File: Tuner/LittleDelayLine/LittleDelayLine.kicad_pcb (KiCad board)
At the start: 2 copper layers, 100 x 100 mm, 115 parts, among them J1 Conn_Coaxial, J10 Conn_Coaxial, J11 Conn_02x05_Odd_Even, J12 Conn_01x01, J13 Conn_01x01, J14 Conn_01x01, J15 Conn_01x01, J16 Conn_01x01, J17 Conn_Coaxial, J18 Conn_01x01, J19 Conn_01x01, J2 Conn_Coaxial, J20 Conn_01x01, J21 Conn_01x01, J22 Conn_Coaxial, J23 Conn_Coaxial, J24 Conn_Coaxial, J25 Conn_01x01, J26 Conn_01x01, J27 Conn_01x01, J28 Conn_01x01, J3 Conn_Coaxial, J4 Conn_Coaxial, J5 Conn_Coaxial, J6 Conn_Coaxial, J7 Conn_Coaxial, J8 Conn_Coaxial, J9 Conn_Coaxial, P10 Conn_01x01, P11 Conn_01x01, P12 Conn_01x01, P2 Conn_01x01, P3 Conn_01x01, P4 Conn_01x01, P5 Conn_01x01, P6 Conn_01x01, P7 Conn_01x01, P8 Conn_01x01, P9 Conn_01x01, U1 MCP23008, U2 ULN2803A

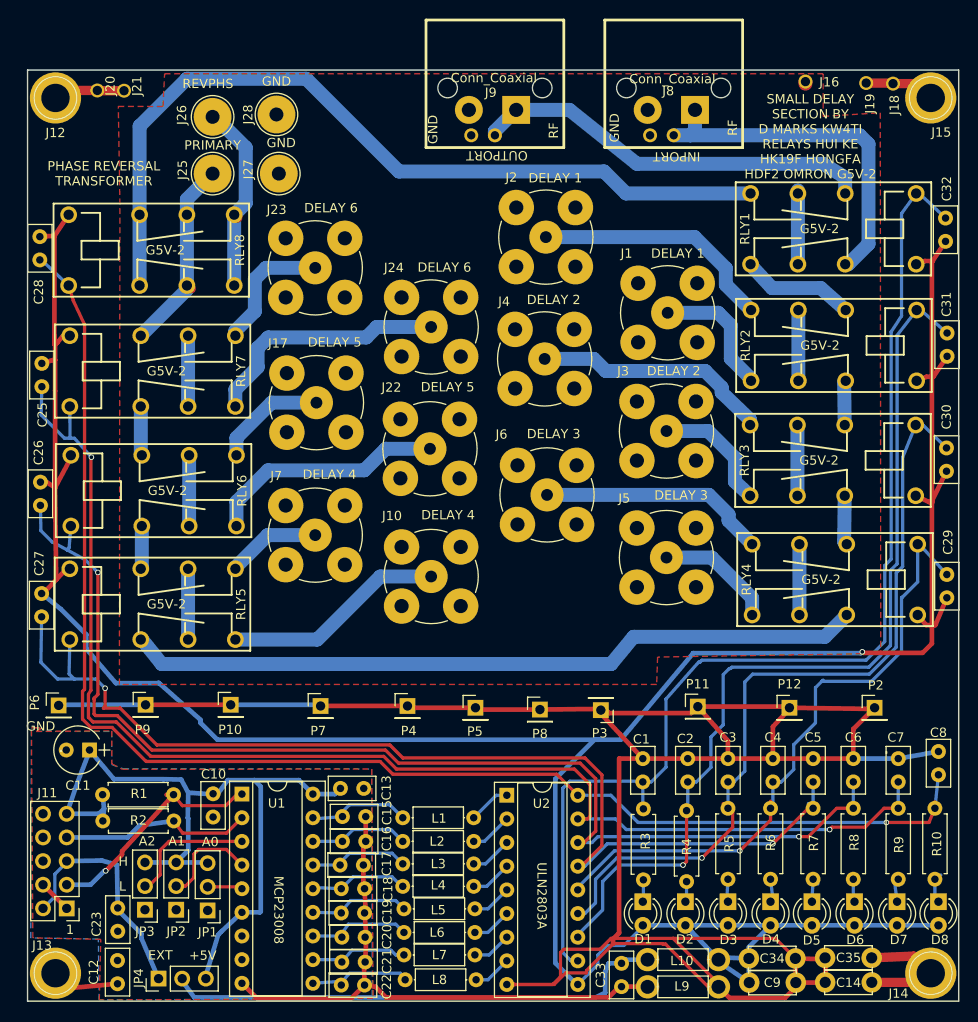
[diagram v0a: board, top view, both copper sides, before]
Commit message: Fixed spacing between BNC connectors in Delay Lines
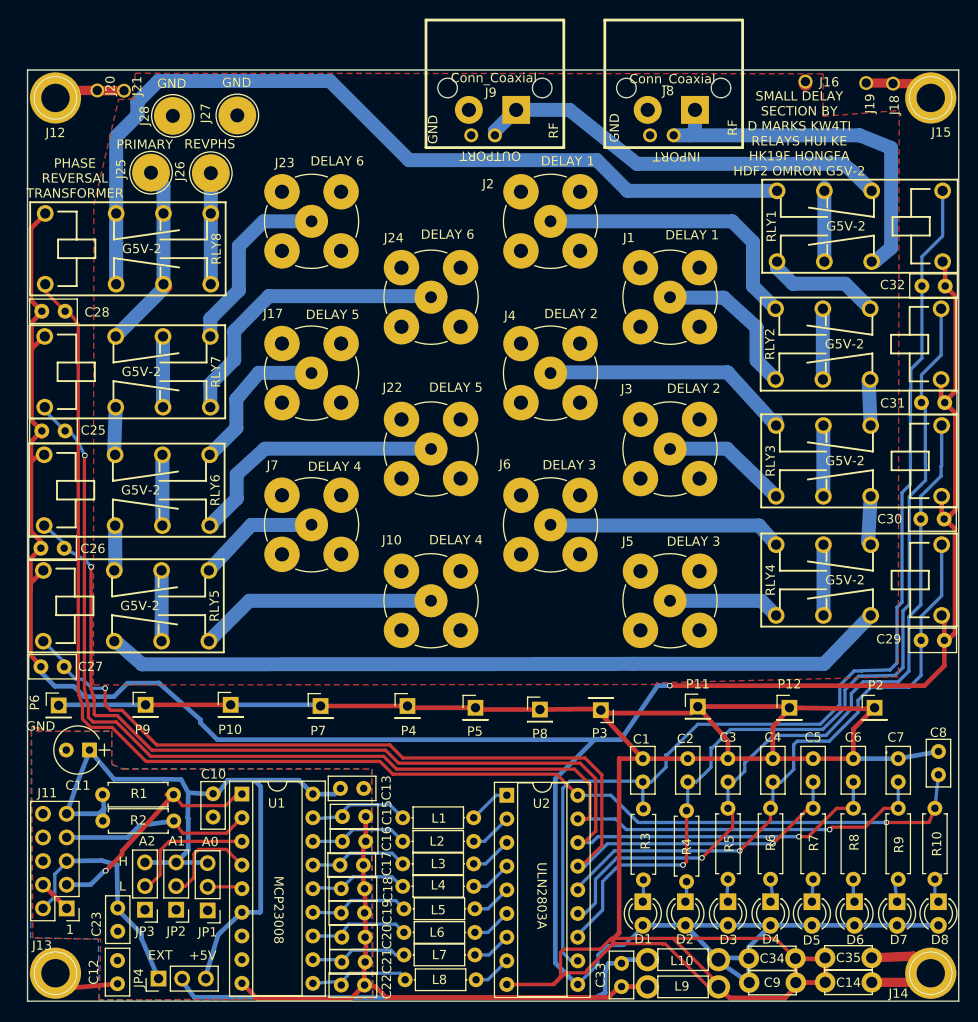
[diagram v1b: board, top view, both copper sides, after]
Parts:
- moved J28 11.1 mm to (65.6, 54.9)
- moved C28 8.02 mm to (51.5, 75.9), turned to 0 degrees
- moved C27 7.86 mm to (51.4, 114.1), turned to 0 degrees
- moved J27 7.68 mm to (72.5, 54.9)
- moved C25 7.25 mm to (51.5, 88.8), turned to 0 degrees
- moved C26 7.10 mm to (51.4, 101.4), turned to 0 degrees
- moved J25 6.62 mm to (63.3, 61.0)
- moved J26 6.05 mm to (69.7, 61.1)
- moved C30 5.14 mm to (148.4, 98.2), turned to 180 degrees
- moved J23 5.01 mm to (80.5, 66.2)
- moved C31 4.98 mm to (148.5, 85.7), turned to 180 degrees
- moved C32 4.80 mm to (148.6, 73.2), turned to 180 degrees
- moved J5 4.65 mm to (119.0, 107.0)
- moved C29 4.58 mm to (148.5, 111.3), turned to 180 degrees
- moved J6 3.24 mm to (106.2, 98.8)
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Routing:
- net RLY5: track 118.7 -> 109.8 mm
- net Net-(J26-Pad1): track 20.4 -> 12.1 mm
- net RLY7: track 143.3 -> 136.6 mm
- net Net-(J23-Pad1): track 13.9 -> 20.6 mm
- net RLY6: track 127.2 -> 121.7 mm
- net RFTHRU: track 89.9 -> 95.0 mm
- net Net-(J24-Pad1): track 26.8 -> 31.8 mm
- net Net-(RLY4-Pad2): track 79.4 -> 84.4 mm
- net RLYPWR: track 320.3 -> 315.7 mm
- net Net-(J2-Pad1): track 26.3 -> 30.8 mm
- net Net-(J17-Pad1): track 12.0 -> 16.4 mm
- net RLY3: track 86.7 -> 82.7 mm
- net Net-(J22-Pad1): track 25.7 -> 29.0 mm
- net Net-(J7-Pad1): track 10.2 -> 13.4 mm
- net Net-(J1-Pad1): track 14.2 -> 17.1 mm
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
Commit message: JLCPCB order 2019-03-25
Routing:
- net GND: track 68.2 -> 233.2 mm, vias 0 -> 24

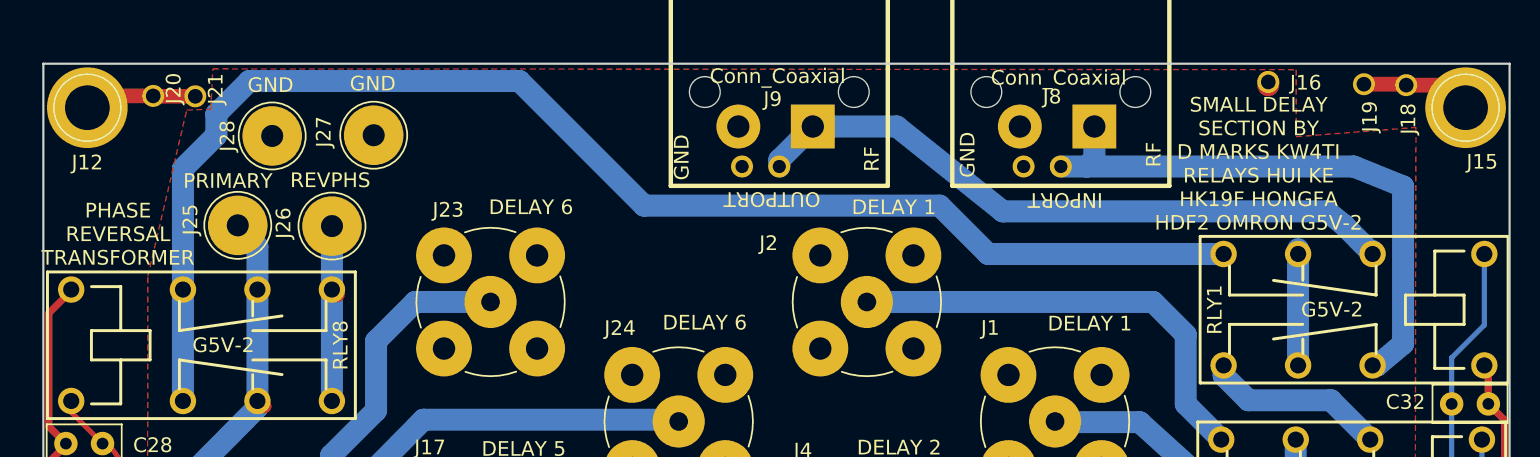
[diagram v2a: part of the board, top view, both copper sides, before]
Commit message: Added extra capacitors between relay power and ground posts
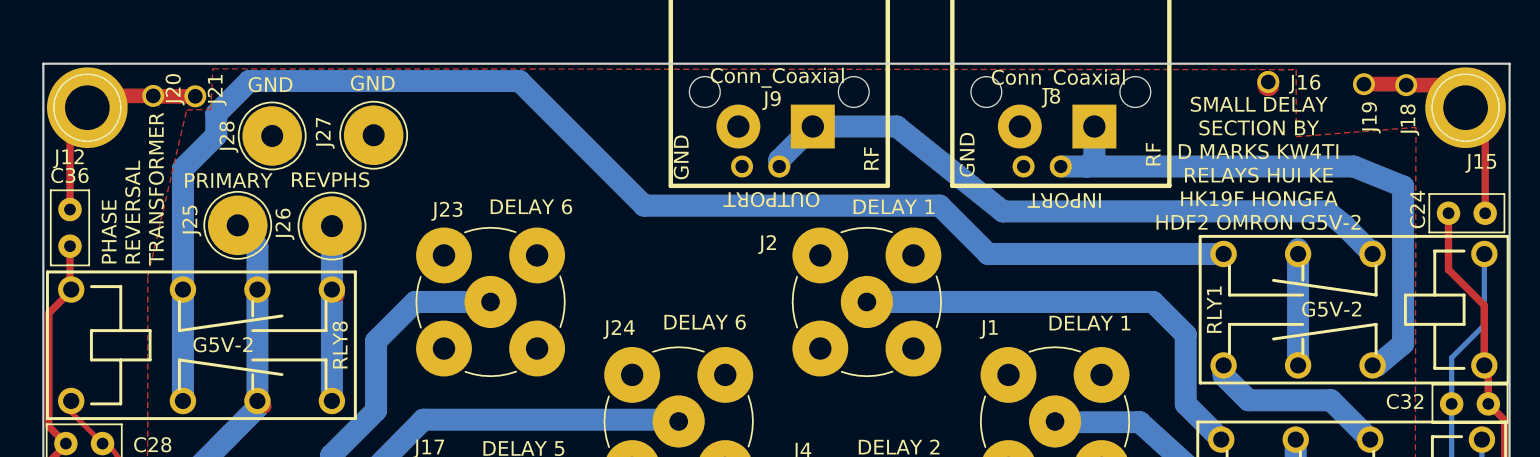
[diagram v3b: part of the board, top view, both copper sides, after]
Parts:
- added C24: 10 nF, Capacitors_THT:C_Disc_D5.0mm_W2.5mm_P2.50mm, F.Cu at (148.3, 60.2)
- added C36: 10 nF, Capacitors_THT:C_Disc_D5.0mm_W2.5mm_P2.50mm, F.Cu at (51.8, 59.9)
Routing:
- net RLYPWR: track 315.7 -> 330.1 mm
- net Net-(C24-Pad1): track 8.59 -> 16.3 mm
- net Net-(C36-Pad1): track 9.29 -> 16.7 mm

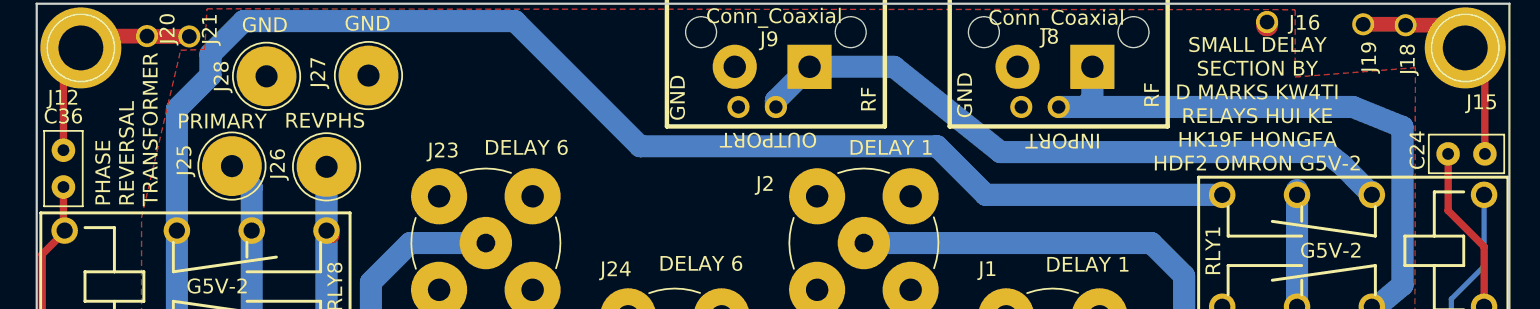
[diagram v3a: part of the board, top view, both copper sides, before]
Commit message: Added extra mounting holes to ground ReversibleLittleSection
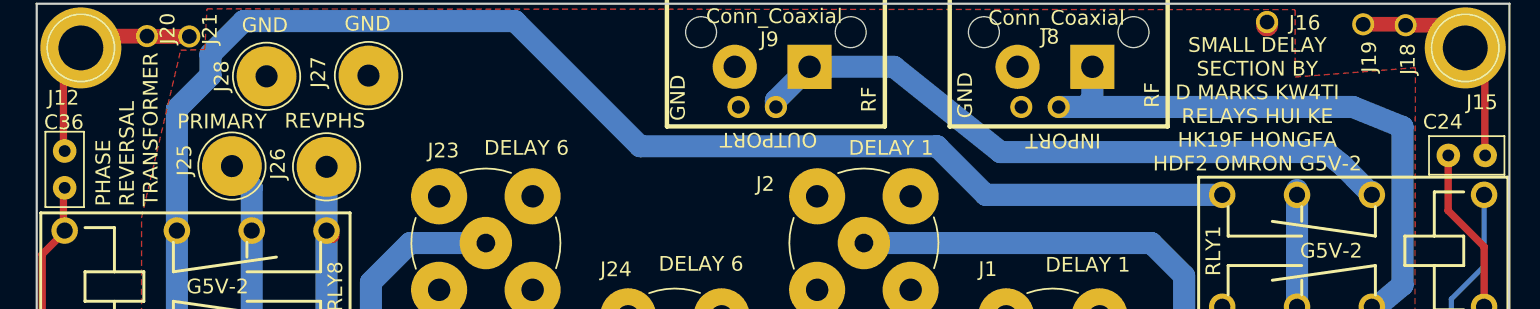
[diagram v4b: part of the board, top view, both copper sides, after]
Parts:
- C24, C36: value 10 nF -> NC
- moved C24 0.10 mm to (148.3, 60.3)
- moved C36 0.10 mm to (51.9, 60.0)
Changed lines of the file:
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@@
   )
   (setup
-    (last_trace_width 0.5)
+    (last_trace_width 0.25)
     (user_trace_width 0.35)
     (user_trace_width 0.5)
@@
   )
   (module Capacitors_THT:C_Disc_D5.0mm_W2.5mm_P2.50mm (layer F.Cu)
-    (at 148.336 60.198 180)
+    (at 148.35 60.3 180)
     (descr "C, Disc series, Radial, pin pitch=2.50mm, , diameter*width=5*2.5mm^2, Capacitor, http://cdn-reichelt.de/documents/datenblatt/B300/DS_KERKO_TC.pdf")
     (tags "C Disc series Radial pin pitch 2.50mm  diameter 5mm width 2.5mm Capacitor")
-    (fp_text reference C24 (at 4.572 0.254 270) (layer F.SilkS)
+    (fp_text reference C24 (at 2.875 2.275 180) (layer F.SilkS)
       (effects (font (size 1 1) (thickness 0.15)))
     )
-    (fp_text value "10 nF" (at 1.25 2.56 180) (layer F.Fab)
+    (fp_text value NC (at 1.25 2.56 180) (layer F.Fab)
       (effects (font (size 1 1) (thickness 0.15)))
     )
@@
   )
   (module Capacitors_THT:C_Disc_D5.0mm_W2.5mm_P2.50mm (layer F.Cu)
-    (at 51.816 59.944 270)
+    (at 51.9 60 270)
     (descr "C, Disc series, Radial, pin pitch=2.50mm, , diameter*width=5*2.5mm^2, Capacitor, http://cdn-reichelt.de/documents/datenblatt/B300/DS_KERKO_TC.pdf")
     (tags "C Disc series Radial pin pitch 2.50mm  diameter 5mm width 2.5mm Capacitor")
-    (fp_text reference C36 (at -2.286 0 360) (layer F.SilkS)
+    (fp_text reference C36 (at -1.95 0.05 360) (layer F.SilkS)
       (effects (font (size 1 1) (thickness 0.15)))
     )
-    (fp_text value "10 nF" (at 1.25 2.56 270) (layer F.Fab)
+    (fp_text value NC (at 1.25 2.56 270) (layer F.Fab)
       (effects (font (size 1 1) (thickness 0.15)))
     )
@@
   (segment (start 101.473 148.209) (end 102.108 148.209) (width 0.35) (layer F.Cu) (net 31) (status 30))
   (segment (start 123.4821 148.1709) (end 123.4821 147.7899) (width 0.35) (layer F.Cu) (net 31) (status 30))
-  (segment (start 148.2776 70.5766) (end 148.2776 66.4896) (width 0.5) (layer F.Cu) (net 32) (status 400000))
-  (segment (start 145.836 64.048) (end 145.836 60.198) (width 0.5) (layer F.Cu) (net 32) (status 800000))
-  (segment (start 148.2776 66.4896) (end 145.836 64.048) (width 0.5) (layer F.Cu) (net 32))
   (segment (start 51.816 62.444) (end 51.816 65.3185) (width 0.5) (layer F.Cu) (net 32) (status 10))
+  (segment (start 148.2776 70.5766) (end 148.2776 66.4896) (width 0.5) (layer F.Cu) (net 32))
+  (segment (start 148.2776 66.4896) (end 145.836 64.048) (width 0.5) (layer F.Cu) (net 32))
+  (segment (start 145.836 64.048) (end 145.836 60.198) (width 0.5) (layer F.Cu) (net 32))
   (segment (start 51.816 65.3185) (end 51.8998 65.4023) (width 0.5) (layer F.Cu) (net 32))
   (segment (start 148.463 111.252) (end 148.463 113.9825) (width 0.5) (layer F.Cu) (net 32))
@@
   (segment (start 59.5198 57.1551) (end 61.7982 54.8767) (width 1.5) (layer B.Cu) (net 76))
   (segment (start 59.5198 73.0023) (end 59.5198 65.4023) (width 1.5) (layer B.Cu) (net 76) (status 30))
-  (segment (start 148.336 60.198) (end 148.336 54.336) (width 0.5) (layer F.Cu) (net 77) (status C00000))
-  (segment (start 148.336 54.336) (end 147 53) (width 0.5) (layer F.Cu) (net 77) (status C00000))
+  (segment (start 148.336 60.198) (end 148.336 54.336) (width 0.5) (layer F.Cu) (net 77))
+  (segment (start 148.336 54.336) (end 147 53) (width 0.5) (layer F.Cu) (net 77))
   (segment (start 140.0683 51.3969) (end 142.8877 51.3969) (width 1) (layer F.Cu) (net 77) (status 30))
   (segment (start 142.8877 51.3969) (end 142.9512 51.4604) (width 1) (layer F.Cu) (net 77) (status 30))
@@
   (segment (start 145.4604 51.4604) (end 147 53) (width 1) (layer F.Cu) (net 77) (status 30))
   (segment (start 146.2986 52.2986) (end 147 53) (width 1) (layer F.Cu) (net 77) (status 30))
-  (segment (start 51.816 59.944) (end 51.816 54.184) (width 0.5) (layer F.Cu) (net 78) (status 10))
   (segment (start 51.816 54.184) (end 53 53) (width 0.5) (layer F.Cu) (net 78))
   (segment (start 57.4929 52.197) (end 53.803 52.197) (width 1) (layer F.Cu) (net 78) (status 30))
@@
   (segment (start 53 53) (end 53 53.3625) (width 0.5) (layer F.Cu) (net 78) (status 30))
   (segment (start 52.13604 53.86396) (end 53 53) (width 1) (layer F.Cu) (net 78) (status 30))
+  (segment (start 51.816 59.944) (end 51.816 54.184) (width 0.5) (layer F.Cu) (net 78) (status 10))
   (zone (net 10) (net_name GND) (layer F.Cu) (hatch edge 0.508)
     (connect_pads (clearance 0.5))
